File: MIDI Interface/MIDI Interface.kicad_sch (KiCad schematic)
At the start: 11 parts

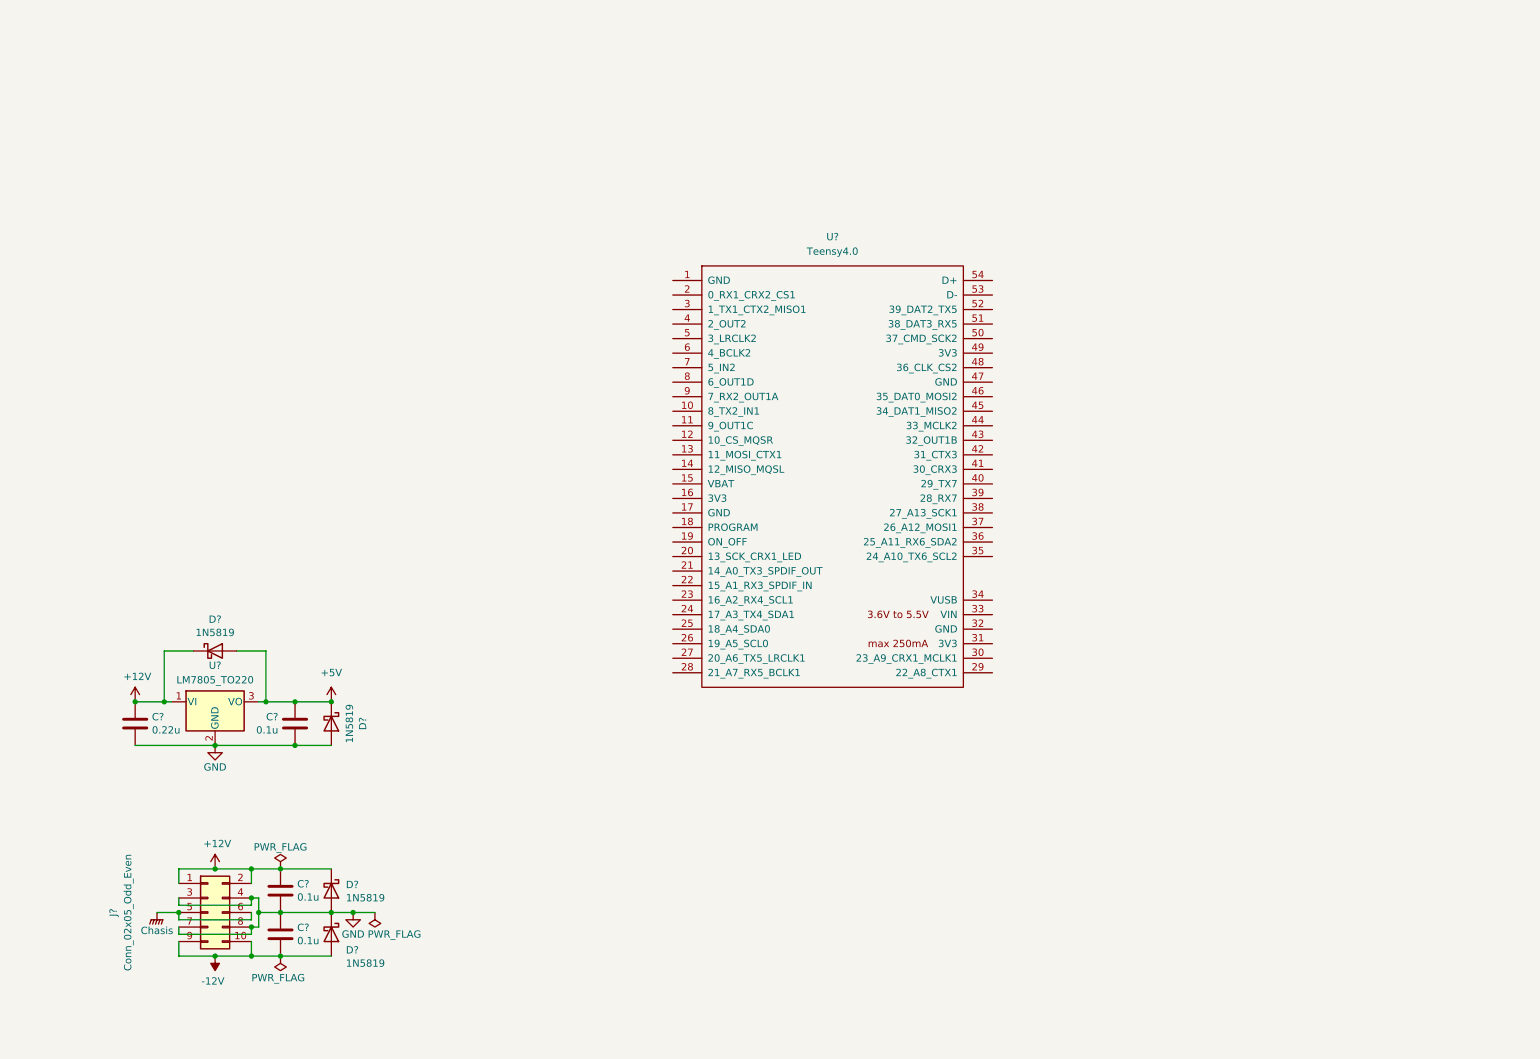
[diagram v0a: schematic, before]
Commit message: Start MIDI interface
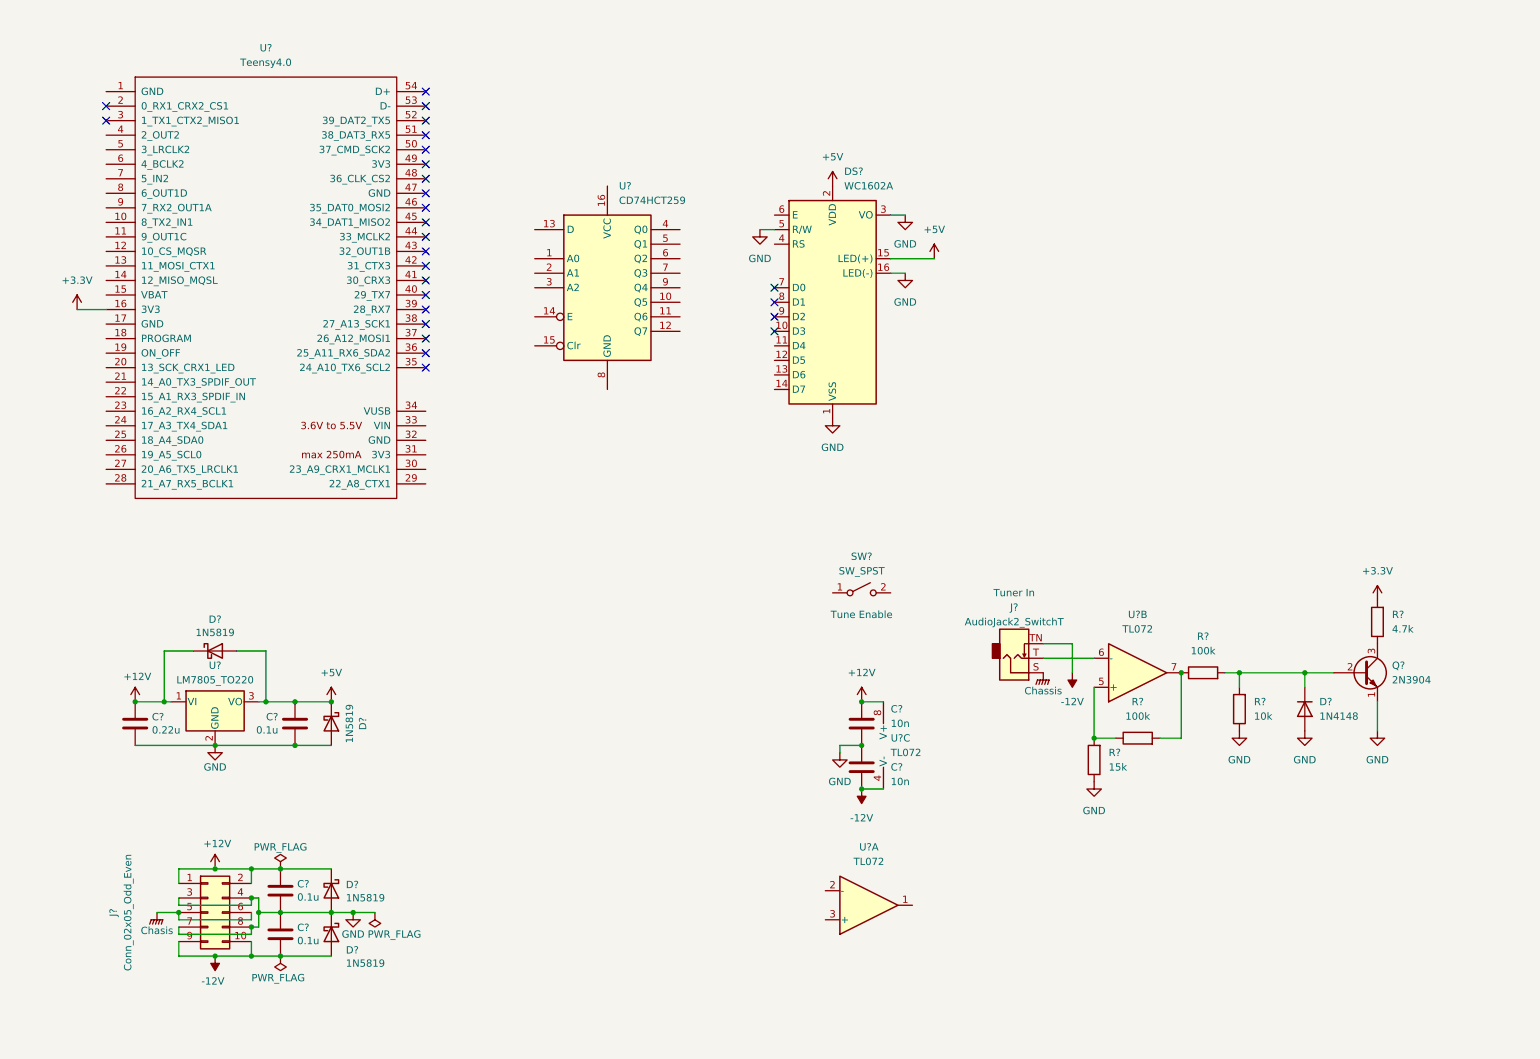
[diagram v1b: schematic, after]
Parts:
- added C? (x2): 10n, symbol Device:C
- added D?: 1N4148, Diode_THT:D_DO-35_SOD27_P7.62mm_Horizontal, symbol Diode:1N4148
- added DS?: WC1602A, Display:WC1602A, symbol Custom:MOP-AL162A
- added J?: AudioJack2_SwitchT, Connector_Audio:Jack_3.5mm_QingPu_WQP-PJ398SM_Vertical_CircularHoles, symbol Connector:AudioJack2_SwitchT
- added Q?: 2N3904, Package_TO_SOT_THT:TO-92_Inline, symbol Transistor_BJT:2N3904
- added R?: 10k, symbol Device:R
- added R? (x2): 100k, symbol Device:R
- added R?: 4.7k, symbol Device:R
- added R?: 15k, symbol Device:R
- added SW?: SW_SPST, symbol Switch:SW_SPST
- added U?: CD74HCT259, symbol Custom:CD74HCT259
- added U? (x3): TL072, symbol Amplifier_Operational:TL072
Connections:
- net +12V: now also C?.2, U?.8 (V+)
- net +5V: now also DS?.15 (LED(+)), DS?.2 (VDD)
- net -12V: now also C?.1, J?.TN, U?.4 (V-)
- net GND: now also C?.1, C?.2, D?.2 (A), DS?.1 (VSS), DS?.16 (LED(-)), DS?.3 (VO), DS?.5 (R/W), Q?.1 (E), R?.1, R?.1
- net +3.3V: now reaches U?.16 (3V3)
- net +3.3V: now also R?.2
- new net: D?.1 (K), Q?.2 (B), R?.2, R?.2
- new net: Q?.3 (C), R?.1
- new net: R?.1, R?.2, U?.5 (+)
- new net: R?.1, R?.2, U?.7
- new net: J?.T, U?.6 (-)
- new net Chassis: J?.S
- no-connect marks 0 -> 26
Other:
- moved on the sheet: U?

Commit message: Finish MIDI interface schematics, minor EG/VCO changes
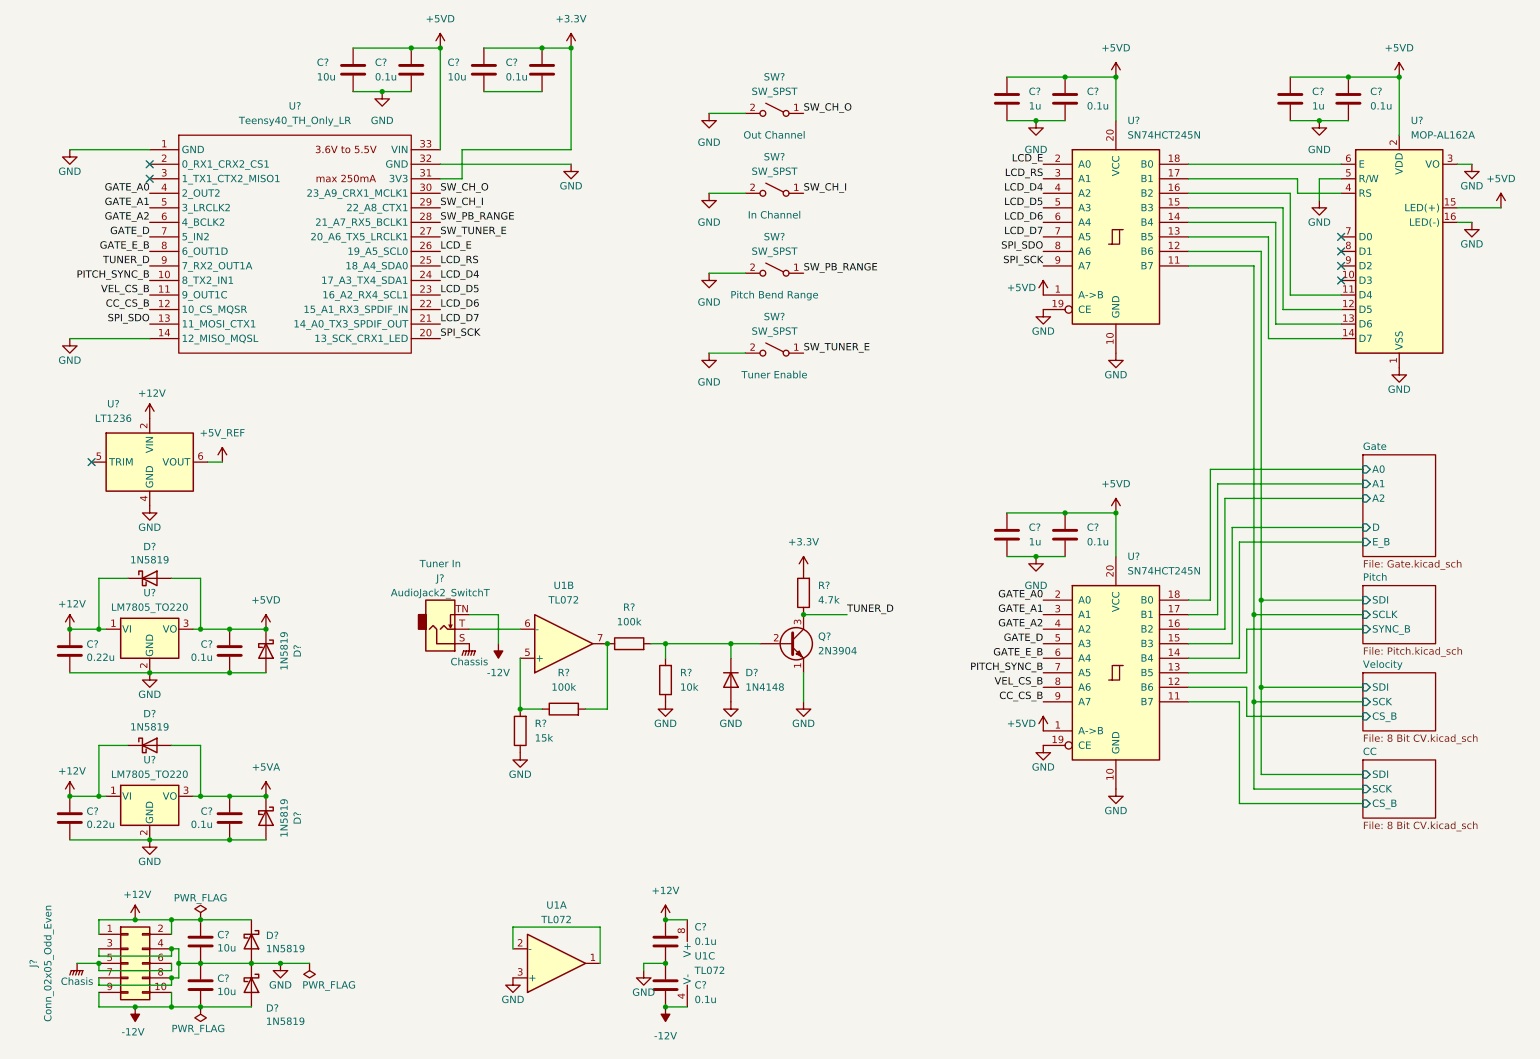
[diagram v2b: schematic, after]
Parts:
- removed DS?: WC1602A, Display:WC1602A, symbol Custom:MOP-AL162A
- removed U?: Teensy4.0, symbol teensy:Teensy4.0
- removed U?: CD74HCT259, symbol Custom:CD74HCT259
- added C? (x5): 0.1u, symbol Device:C
- added C?: 0.1u, Capacitor_THT:C_Disc_D5.0mm_W2.5mm_P5.00mm, symbol Device:C
- added C? (x3): 1u, symbol Device:C
- added C? (x2): 10u, symbol Device:C
- added C?: 0.22u, Capacitor_THT:C_Disc_D5.0mm_W2.5mm_P5.00mm, symbol Device:C
- added D? (x2): 1N5819, Diode_THT:D_DO-41_SOD81_P10.16mm_Horizontal, symbol Diode:1N5819
- added SW? (x3): SW_SPST, symbol Switch:SW_SPST
- added U? (x2): SN74HCT245N, symbol 74xx:74HC245
- added U?: LM7805_TO220, Package_TO_SOT_THT:TO-220-3_Vertical, symbol Regulator_Linear:LM7805_TO220
- added U?: Teensy40_TH_Only_LR, symbol Custom:Teensy40_TH_Only_LR
- added U?: LT1236, symbol Custom:LT1236
- added U?: MOP-AL162A, symbol Custom:MOP-AL162A
- C? (x2): value 0.1u -> 10u
- C? (x2): value 10n -> 0.1u
- SW?: Notes Tune Enable -> Tuner Enable
- gave numbers to parts that had none: 1
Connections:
- net +12V: now also C?.1, D?.1 (K), U?.1 (VI), U?.2 (VIN)
- net +3.3V: now also C?.1, C?.1, U?.31 (3V3)
- net GND: now also SW?.2 (B), U1.3 (+), C?.2, C?.2, C?.2, C?.2, C?.2, C?.2, C?.2, C?.2, C?.2, C?.2, D?.2 (A), SW?.2 (B), SW?.2 (B), SW?.2 (B), U?.1 (GND), U?.1 (VSS), U?.10 (GND), U?.10 (GND), U?.14 (12_MISO_MQSL), U?.16 (LED(-)), U?.19 (CE), U?.19 (CE), U?.2 (GND), U?.3 (VO), U?.32 (GND), U?.4 (GND), U?.5 (R/W)
- net TUNER_D: now reaches Q?.3 (C), R?.1
- net TUNER_D: now also U?.9 (7_RX2_OUT1A)
- net SW_TUNER_E: now reaches SW?.1 (A)
- net SW_TUNER_E: now also U?.27 (20_A6_TX5_LRCLK1)
- net at U1.1: now also U1.2 (-)
- net +5V renamed +5VD
- net +5VD: now also C?.1, C?.1, C?.1, C?.1, C?.1, C?.1, C?.1, C?.1, U?.1 (A->B), U?.1 (A->B), U?.15 (LED(+)), U?.2 (VDD), U?.20 (VCC), U?.20 (VCC), U?.33 (VIN)
- new net: C?.2, C?.2
- new net: U?.13 (B5), U?.14 (D7)
- new net: U?.13 (D6), U?.14 (B4)
- new net: U?.12 (D5), U?.15 (B3)
- new net: U?.11 (D4), U?.16 (B2)
- new net: U?.17 (B1), U?.4 (RS)
- new net: U?.18 (B0), U?.6 (E)
- new net +5VA: C?.1, D?.1 (K), D?.2 (A), U?.3 (VO)
- new net +5V_REF: U?.6 (VOUT)
- new net CC/CS_B: U?.11 (B7)
- new net CC/SCK: U?.11 (B7)
- new net CC/SDI: U?.12 (B6)
- new net CC_CS_B: U?.12 (10_CS_MQSR), U?.9 (A7)
- new net GATE_A0: U?.2 (A0), U?.4 (2_OUT2)
- new net GATE_A1: U?.3 (A1), U?.5 (3_LRCLK2)
- new net GATE_A2: U?.4 (A2), U?.6 (4_BCLK2)
- new net GATE_D: U?.5 (A3), U?.7 (5_IN2)
- new net GATE_E_B: U?.6 (A4), U?.8 (6_OUT1D)
- new net Gate/A0: U?.18 (B0)
- new net Gate/A1: U?.17 (B1)
- new net Gate/A2: U?.16 (B2)
- new net Gate/D: U?.15 (B3)
- new net Gate/E_B: U?.14 (B4)
- new net LCD_D4: U?.24 (17_A3_TX4_SDA1), U?.4 (A2)
- new net LCD_D5: U?.23 (16_A2_RX4_SCL1), U?.5 (A3)
- new net LCD_D6: U?.22 (15_A1_RX3_SPDIF_IN), U?.6 (A4)
- new net LCD_D7: U?.21 (14_A0_TX3_SPDIF_OUT), U?.7 (A5)
- new net LCD_E: U?.2 (A0), U?.26 (19_A5_SCL0)
- new net LCD_RS: U?.25 (18_A4_SDA0), U?.3 (A1)
- new net PITCH_SYNC_B: U?.10 (8_TX2_IN1), U?.7 (A5)
- new net Pitch/SYNC_B: U?.13 (B5)
- new net SPI_SCK: U?.20 (13_SCK_CRX1_LED), U?.9 (A7)
- new net SPI_SDO: U?.13 (11_MOSI_CTX1), U?.8 (A6)
- new net SW_CH_I: SW?.1 (A), U?.29 (22_A8_CTX1)
- new net SW_CH_O: SW?.1 (A), U?.30 (23_A9_CRX1_MCLK1)
- new net SW_PB_RANGE: SW?.1 (A), U?.28 (21_A7_RX5_BCLK1)
- new net VEL_CS_B: U?.11 (9_OUT1C), U?.8 (A6)
- new net Velocity/CS_B: U?.12 (B6)
- no-connect marks 26 -> 7
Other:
- added sheet CC (8 Bit CV.kicad_sch)
- added sheet Gate (Gate.kicad_sch)
- added sheet Pitch (Pitch.kicad_sch)
- added sheet Velocity (8 Bit CV.kicad_sch)
- moved on the sheet: C?, D?, J?, Q?, R?, SW?, U1A, U1B, U1C, U?

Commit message: Fix MIDI I/F ERC issues, add tuner OVP
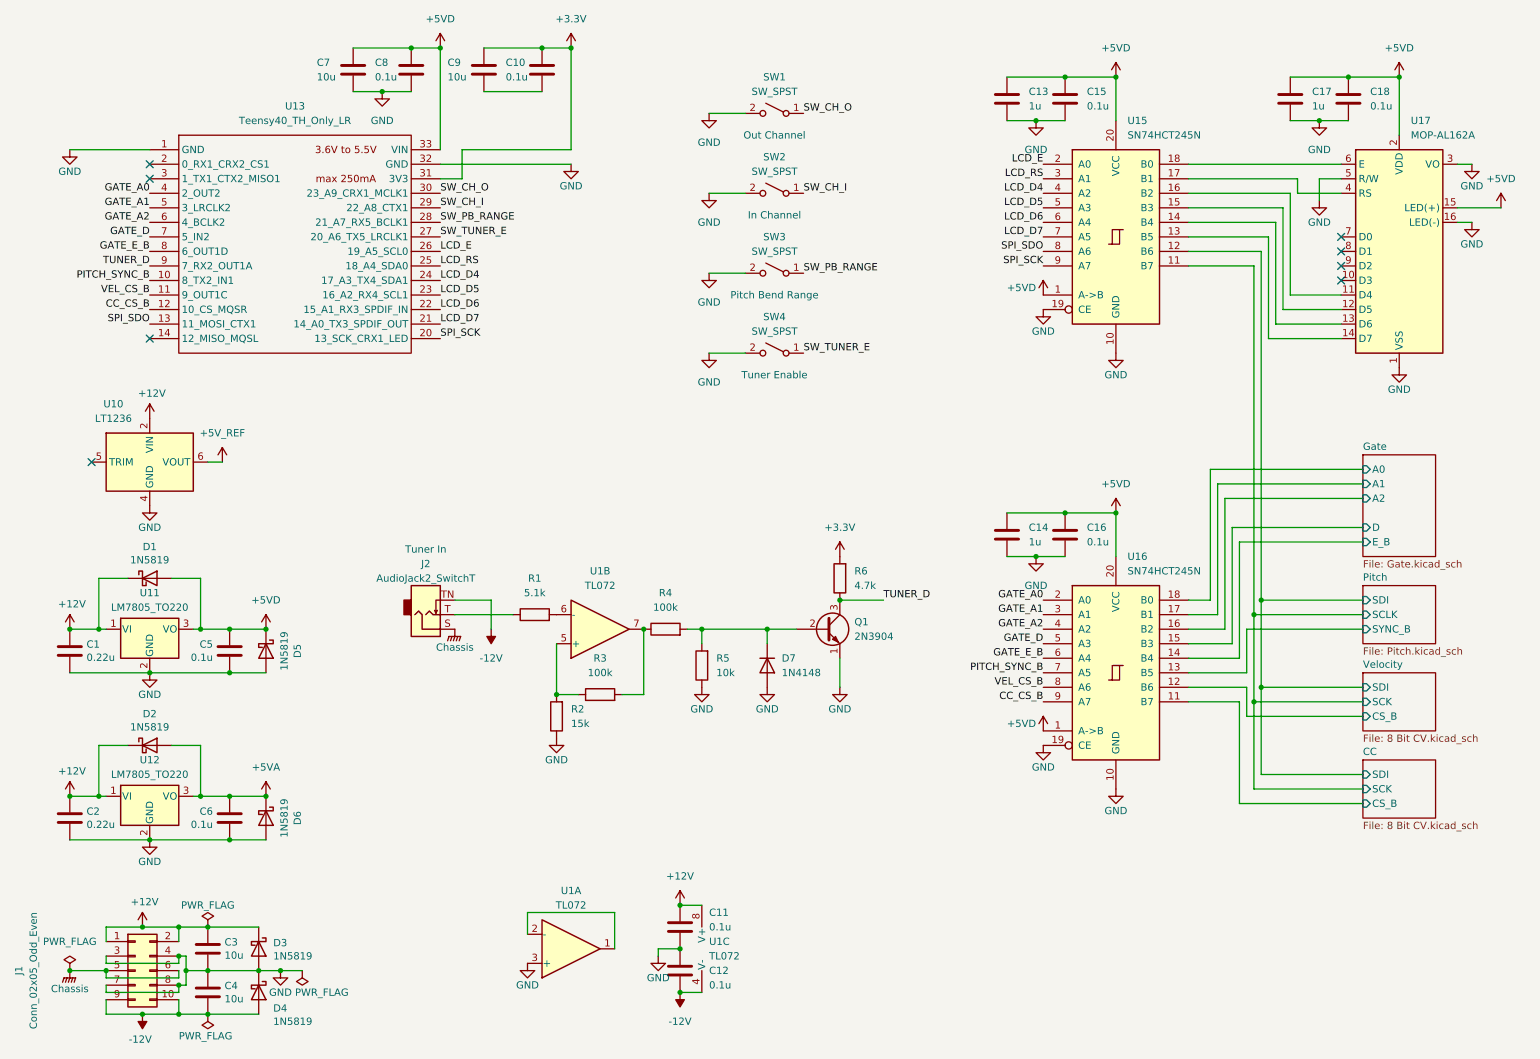
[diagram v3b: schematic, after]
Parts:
- removed C? (x2): 10u, Capacitor_THT:C_Disc_D5.0mm_W2.5mm_P5.00mm, symbol Device:C
- removed D? (x2): 1N5819, Diode_THT:D_DO-41_SOD81_P10.16mm_Horizontal, symbol Diode:1N5819
- removed J?: Conn_02x05_Odd_Even, Connector_PinHeader_2.54mm:PinHeader_2x05_P2.54mm_Vertical, symbol Connector_Generic:Conn_02x05_Odd_Even
- added C3, C4: 10u, Capacitor_THT:C_Disc_D5.0mm_W2.5mm_P5.00mm, symbol Device:C
- added D3, D4: 1N5819, Diode_THT:D_DO-41_SOD81_P10.16mm_Horizontal, symbol Diode:1N5819
- added J1: Conn_02x05_Odd_Even, Connector_PinHeader_2.54mm:PinHeader_2x05_P2.54mm_Vertical, symbol Connector_Generic:Conn_02x05_Odd_Even
- added R1: 5.1k, symbol Device:R
- gave numbers to parts that had none: 39
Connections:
- net +12V: now also C3.1, D3.1 (K), J1.1 (Pin_1), J1.2 (Pin_2)
- net -12V: now also C4.2, D4.2 (A), J1.10 (Pin_10), J1.9 (Pin_9)
- net Chassis: now also J1.5 (Pin_5), J1.6 (Pin_6)
- net GND: now also C3.2, C4.1, D3.2 (A), D4.1 (K), J1.3 (Pin_3), J1.4 (Pin_4), J1.7 (Pin_7), J1.8 (Pin_8); no longer U13.14 (12_MISO_MQSL)
- net at J2.T: now also R1.1; no longer U1.6 (-)
- new net: R1.2, U1.6 (-)
- no-connect marks 7 -> 8
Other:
- moved on the sheet: C11, C12, D7, J2, Q1, R2, R3, R4, R5, R6, U1A, U1B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
